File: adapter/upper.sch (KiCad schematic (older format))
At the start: 8 parts, among them J1 MALE, J2 FEMALE, J3 STANDOFF, J4 STANDOFF

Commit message: Finish schematic
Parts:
- removed D1: Red, symbol Device:LED_Small
- removed D2: Green, symbol Device:LED_Small
- removed J1: MALE, symbol Connector_Generic:Conn_02x02_Counter_Clockwise
- removed J2: FEMALE, symbol Connector_Generic:Conn_02x02_Counter_Clockwise
- removed J3, J4: STANDOFF, symbol Connector_Generic:Conn_01x01
- removed R1, R2: 1k, symbol Device:R_Small_US
- added J11: MALE, Connector_PinHeader_2.54mm:PinHeader_2x02_P2.54mm_Horizontal, symbol Connector_Generic:Conn_02x02_Top_Bottom
- added J12: FEMALE, Connector_PinSocket_2.54mm:PinSocket_2x02_P2.54mm_Vertical, symbol Connector_Generic:Conn_02x02_Odd_Even
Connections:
- wire segments 21 -> 13
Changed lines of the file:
@@
 Comment4 ""
 $EndDescr
-$Comp
-L Connector_Generic:Conn_02x02_Counter_Clockwise J?
-U 1 1 5FA96B2A
-P 3650 1700
-AR Path="/5FA96B2A" Ref="J?"  Part="1"
-AR Path="/5FA6C89B/5FA96B2A" Ref="J?"  Part="1"
-AR Path="/5FA6C6C8/5FA96B2A" Ref="J1"  Part="1"
-F 0 "J1" H 3700 1917 50  0000 C CNN
-F 1 "MALE" H 3700 1826 50  0000 C CNN
-F 2 "" H 3650 1700 50  0001 C CNN
-F 3 "~" H 3650 1700 50  0001 C CNN
-	1    3650 1700
-	1    0    0    -1
-$EndComp
-$Comp
-L Connector_Generic:Conn_02x02_Counter_Clockwise J?
-U 1 1 5FA96B38
-P 3650 2200
-AR Path="/5FA96B38" Ref="J?"  Part="1"
-AR Path="/5FA6C89B/5FA96B38" Ref="J?"  Part="1"
-AR Path="/5FA6C6C8/5FA96B38" Ref="J2"  Part="1"
-F 0 "J2" H 3700 2417 50  0000 C CNN
-F 1 "FEMALE" H 3700 2326 50  0000 C CNN
-F 2 "" H 3650 2200 50  0001 C CNN
-F 3 "~" H 3650 2200 50  0001 C CNN
-	1    3650 2200
-	1    0    0    -1
-$EndComp
 Wire Wire Line
-	3450 2300 3400 2300
+	5350 2900 5150 2900
 Wire Wire Line
-	3450 2200 3350 2200
+	5150 2900 5150 3500
 Wire Wire Line
-	3450 1800 3400 1800
+	6050 3500 6050 3550
 Wire Wire Line
-	3400 1800 3400 2300
-Wire Wire Line
-	3450 1700 3350 1700
-Wire Wire Line
-	3350 1700 3350 2200
-Wire Wire Line
-	3950 2300 4000 2300
-Wire Wire Line
-	4050 2300 4050 2350
-Wire Wire Line
-	3950 2200 4050 2200
-Wire Wire Line
-	3950 1800 4000 1800
-Wire Wire Line
-	4000 1800 4000 2300
-Connection ~ 4000 2300
-Wire Wire Line
-	4000 2300 4050 2300
-Wire Wire Line
-	3950 1700 4050 1700
-Wire Wire Line
-	4050 1700 4050 2200
+	5850 3000 5950 3000
 $Comp
 L power:+5V #PWR?
-U 1 1 5FA96B54
-P 3350 1650
-AR Path="/5FA6C89B/5FA96B54" Ref="#PWR?"  Part="1"
-AR Path="/5FA6C6C8/5FA96B54" Ref="#PWR?"  Part="1"
-F 0 "#PWR?" H 3350 1500 50  0001 C CNN
-F 1 "+5V" H 3365 1823 50  0000 C CNN
-F 2 "" H 3350 1650 50  0001 C CNN
-F 3 "" H 3350 1650 50  0001 C CNN
-	1    3350 1650
+U 1 1 5FB6CCB3
+P 5150 2900
+AR Path="/5FA6C89B/5FB6CCB3" Ref="#PWR?"  Part="1"
+AR Path="/5FA6C6C8/5FB6CCB3" Ref="#PWR0110"  Part="1"
+F 0 "#PWR0110" H 5150 2750 50  0001 C CNN
+F 1 "+5V" H 5165 3073 50  0000 C CNN
+F 2 "" H 5150 2900 50  0001 C CNN
+F 3 "" H 5150 2900 50  0001 C CNN
+	1    5150 2900
 	1    0    0    -1
 $EndComp
 $Comp
 L power:GND #PWR?
-U 1 1 5FA96B5A
-P 4050 2350
-AR Path="/5FA6C89B/5FA96B5A" Ref="#PWR?"  Part="1"
-AR Path="/5FA6C6C8/5FA96B5A" Ref="#PWR?"  Part="1"
-F 0 "#PWR?" H 4050 2100 50  0001 C CNN
-F 1 "GND" H 4050 2200 50  0000 C CNN
-F 2 "" H 4050 2350 50  0001 C CNN
-F 3 "" H 4050 2350 50  0001 C CNN
-	1    4050 2350
+U 1 1 5FB6CCB9
+P 6050 3550
+AR Path="/5FA6C89B/5FB6CCB9" Ref="#PWR?"  Part="1"
+AR Path="/5FA6C6C8/5FB6CCB9" Ref="#PWR0111"  Part="1"
+F 0 "#PWR0111" H 6050 3300 50  0001 C CNN
+F 1 "GND" H 6050 3400 50  0000 C CNN
+F 2 "" H 6050 3550 50  0001 C CNN
+F 3 "" H 6050 3550 50  0001 C CNN
+	1    6050 3550
 	1    0    0    -1
 $EndComp
 $Comp
-L Connector_Generic:Conn_01x01 J?
-U 1 1 5FA96B62
-P 3200 4300
-AR Path="/5FA6C89B/5FA96B62" Ref="J?"  Part="1"
-AR Path="/5FA6C6C8/5FA96B62" Ref="J3"  Part="1"
-F 0 "J3" V 3350 4250 50  0000 L CNN
-F 1 "STANDOFF" V 3450 4150 50  0000 L CNN
-F 2 "" H 3200 4300 50  0001 C CNN
-F 3 "~" H 3200 4300 50  0001 C CNN
-	1    3200 4300
-	0    1    1    0
-$EndComp
-$Comp
-L Connector_Generic:Conn_01x01 J?
-U 1 1 5FA96B68
-P 4150 4300
-AR Path="/5FA6C89B/5FA96B68" Ref="J?"  Part="1"
-AR Path="/5FA6C6C8/5FA96B68" Ref="J4"  Part="1"
-F 0 "J4" V 4300 4250 50  0000 L CNN
-F 1 "STANDOFF" V 4400 4150 50  0000 L CNN
-F 2 "" H 4150 4300 50  0001 C CNN
-F 3 "~" H 4150 4300 50  0001 C CNN
-	1    4150 4300
-	0    1    1    0
-$EndComp
-$Comp
-L power:+5V #PWR?
-U 1 1 5FA97846
-P 3200 3150
-AR Path="/5FA6C89B/5FA97846" Ref="#PWR?"  Part="1"
-AR Path="/5FA6C6C8/5FA97846" Ref="#PWR?"  Part="1"
-F 0 "#PWR?" H 3200 3000 50  0001 C CNN
-F 1 "+5V" H 3215 3323 50  0000 C CNN
-F 2 "" H 3200 3150 50  0001 C CNN
-F 3 "" H 3200 3150 50  0001 C CNN
-	1    3200 3150
+L Connector_Generic:Conn_02x02_Top_Bottom J?
+U 1 1 5FB6CCC1
+P 5550 2900
+AR Path="/5FB6CCC1" Ref="J?"  Part="1"
+AR Path="/5FA6C89B/5FB6CCC1" Ref="J?"  Part="1"
+AR Path="/5FA6C6C8/5FB6CCC1" Ref="J11"  Part="1"
+F 0 "J11" H 5600 3117 50  0000 C CNN
+F 1 "MALE" H 5600 3026 50  0000 C CNN
+F 2 "Connector_PinHeader_2.54mm:PinHeader_2x02_P2.54mm_Horizontal" H 5550 2900 50  0001 C CNN
+F 3 "~" H 5550 2900 50  0001 C CNN
+	1    5550 2900
 	1    0    0    -1
 $EndComp
 $Comp
-L Device:R_Small_US R1
-U 1 1 5FA97B4B
-P 3200 3450
-F 0 "R1" H 3268 3496 50  0000 L CNN
-F 1 "1k" H 3268 3405 50  0000 L CNN
-F 2 "" H 3200 3450 50  0001 C CNN
-F 3 "~" H 3200 3450 50  0001 C CNN
-	1    3200 3450
-	1    0    0    -1
-$EndComp
-$Comp
-L Device:LED_Small D1
-U 1 1 5FA97E69
-P 3200 3800
-F 0 "D1" V 3246 3730 50  0000 R CNN
-F 1 "Red" V 3155 3730 50  0000 R CNN
-F 2 "" V 3200 3800 50  0001 C CNN
-F 3 "~" V 3200 3800 50  0001 C CNN
-	1    3200 3800
-	0    -1   -1   0
-$EndComp
-Wire Wire Line
-	3200 3150 3200 3350
-Wire Wire Line
-	3200 3550 3200 3700
-Wire Wire Line
-	3200 3900 3200 4100
-$Comp
-L Device:LED_Small D2
-U 1 1 5FA99B4F
-P 4150 3800
-F 0 "D2" V 4196 3730 50  0000 R CNN
-F 1 "Green" V 4105 3730 50  0000 R CNN
-F 2 "" V 4150 3800 50  0001 C CNN
-F 3 "~" V 4150 3800 50  0001 C CNN
-	1    4150 3800
-	0    -1   -1   0
-$EndComp
-$Comp
-L Device:R_Small_US R2
-U 1 1 5FA99CCA
-P 4150 3450
-F 0 "R2" H 4218 3496 50  0000 L CNN
-F 1 "1k" H 4218 3405 50  0000 L CNN
-F 2 "" H 4150 3450 50  0001 C CNN
-F 3 "~" H 4150 3450 50  0001 C CNN
-	1    4150 3450
-	1    0    0    -1
-$EndComp
-$Comp
-L power:+5V #PWR?
-U 1 1 5FA99E18
-P 4150 3150
-AR Path="/5FA6C89B/5FA99E18" Ref="#PWR?"  Part="1"
-AR Path="/5FA6C6C8/5FA99E18" Ref="#PWR?"  Part="1"
-F 0 "#PWR?" H 4150 3000 50  0001 C CNN
-F 1 "+5V" H 4165 3323 50  0000 C CNN
-F 2 "" H 4150 3150 50  0001 C CNN
-F 3 "" H 4150 3150 50  0001 C CNN
-	1    4150 3150
+L Connector_Generic:Conn_02x02_Odd_Even J?
+U 1 1 5FB6CCC7
+P 5550 3400
+AR Path="/5FB6CCC7" Ref="J?"  Part="1"
+AR Path="/5FA6C89B/5FB6CCC7" Ref="J?"  Part="1"
+AR Path="/5FA6C6C8/5FB6CCC7" Ref="J12"  Part="1"
+F 0 "J12" H 5600 3617 50  0000 C CNN
+F 1 "FEMALE" H 5600 3526 50  0000 C CNN
+F 2 "Connector_PinSocket_2.54mm:PinSocket_2x02_P2.54mm_Vertical" H 5550 3400 50  0001 C CNN
+F 3 "~" H 5550 3400 50  0001 C CNN
+	1    5550 3400
 	1    0    0    -1
 $EndComp
 Wire Wire Line
-	4150 3350 4150 3150
+	5850 3500 6050 3500
 Wire Wire Line
-	4150 3550 4150 3700
+	5850 3400 5950 3400
 Wire Wire Line
-	4150 3900 4150 4100
+	5950 3000 5950 3400
 Wire Wire Line
-	3350 1650 3350 1700
-Connection ~ 3350 1700
+	5850 2900 6050 2900
+Wire Wire Line
+	6050 2900 6050 3500
+Connection ~ 6050 3500
+Connection ~ 5150 2900
+Wire Wire Line
+	5350 3000 5250 3000
+Wire Wire Line
+	5150 3500 5350 3500
+Wire Wire Line
+	5250 3000 5250 3400
+Wire Wire Line
+	5250 3400 5350 3400
 $EndSCHEMATC

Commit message: Change female headers to horizontal
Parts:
- J12: footprint Connector_PinSocket_2.54mm:PinSocket_2x02_P2.54mm_Vertical -> Connector_PinSocket_2.54mm:PinSocket_2x02_P2.54mm_Horizontal
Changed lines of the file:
@@
 F 0 "J12" H 5600 3617 50  0000 C CNN
 F 1 "FEMALE" H 5600 3526 50  0000 C CNN
-F 2 "Connector_PinSocket_2.54mm:PinSocket_2x02_P2.54mm_Vertical" H 5550 3400 50  0001 C CNN
+F 2 "Connector_PinSocket_2.54mm:PinSocket_2x02_P2.54mm_Horizontal" H 5550 3400 50  0001 C CNN
 F 3 "~" H 5550 3400 50  0001 C CNN
 	1    5550 3400

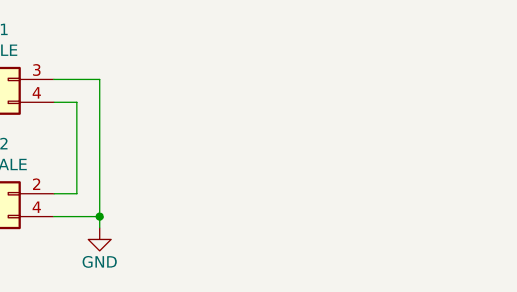
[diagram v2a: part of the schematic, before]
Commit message: Add holes for standoffs
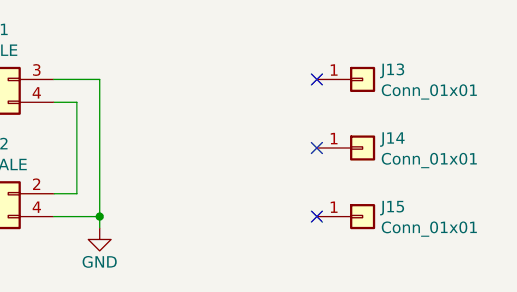
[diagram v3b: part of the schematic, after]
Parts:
- added J13, J14, J15: Conn_01x01, MountingHole:MountingHole_2.2mm_M2_Pad_Via, symbol Connector_Generic:Conn_01x01
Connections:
- no-connect marks 0 -> 3
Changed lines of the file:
@@
 Wire Wire Line
 	5250 3400 5350 3400
+$Comp
+L Connector_Generic:Conn_01x01 J?
+U 1 1 5FB93146
+P 7200 2900
+AR Path="/5FA6C89B/5FB93146" Ref="J?"  Part="1"
+AR Path="/5FA6C6C8/5FB93146" Ref="J13"  Part="1"
+F 0 "J13" H 7280 2942 50  0000 L CNN
+F 1 "Conn_01x01" H 7280 2851 50  0000 L CNN
+F 2 "MountingHole:MountingHole_2.2mm_M2_Pad_Via" H 7200 2900 50  0001 C CNN
+F 3 "~" H 7200 2900 50  0001 C CNN
+	1    7200 2900
+	1    0    0    -1
+$EndComp
+NoConn ~ 7000 2900
+$Comp
+L Connector_Generic:Conn_01x01 J?
+U 1 1 5FB9314D
+P 7200 3200
+AR Path="/5FA6C89B/5FB9314D" Ref="J?"  Part="1"
+AR Path="/5FA6C6C8/5FB9314D" Ref="J14"  Part="1"
+F 0 "J14" H 7280 3242 50  0000 L CNN
+F 1 "Conn_01x01" H 7280 3151 50  0000 L CNN
+F 2 "MountingHole:MountingHole_2.2mm_M2_Pad_Via" H 7200 3200 50  0001 C CNN
+F 3 "~" H 7200 3200 50  0001 C CNN
+	1    7200 3200
+	1    0    0    -1
+$EndComp
+$Comp
+L Connector_Generic:Conn_01x01 J?
+U 1 1 5FB93153
+P 7200 3500
+AR Path="/5FA6C89B/5FB93153" Ref="J?"  Part="1"
+AR Path="/5FA6C6C8/5FB93153" Ref="J15"  Part="1"
+F 0 "J15" H 7280 3542 50  0000 L CNN
+F 1 "Conn_01x01" H 7280 3451 50  0000 L CNN
+F 2 "MountingHole:MountingHole_2.2mm_M2_Pad_Via" H 7200 3500 50  0001 C CNN
+F 3 "~" H 7200 3500 50  0001 C CNN
+	1    7200 3500
+	1    0    0    -1
+$EndComp
+NoConn ~ 7000 3200
+NoConn ~ 7000 3500
 $EndSCHEMATC

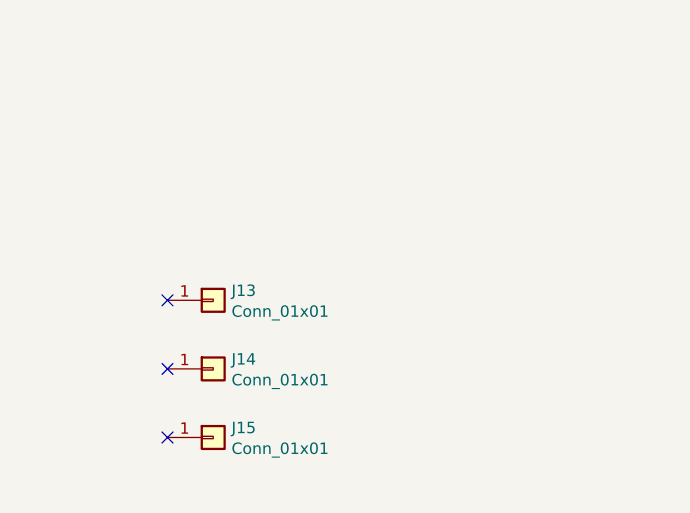
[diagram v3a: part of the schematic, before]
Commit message: Move LEDs to upper board
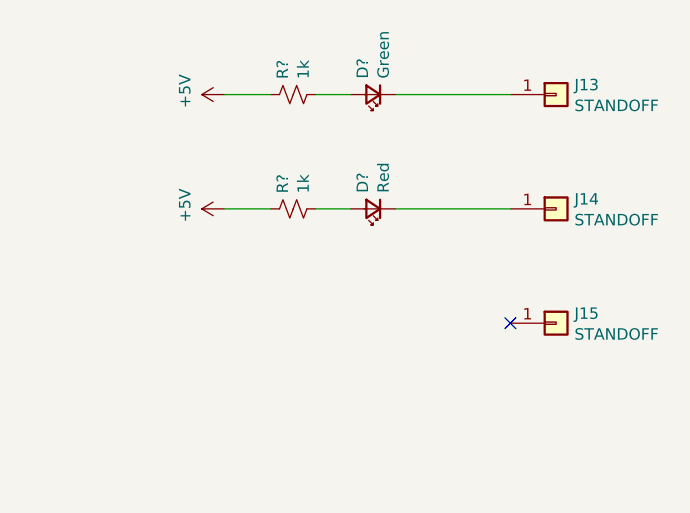
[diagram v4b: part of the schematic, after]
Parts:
- added D?: Red, LED_SMD:LED_0805_2012Metric_Pad1.15x1.40mm_HandSolder, symbol Device:LED_Small
- added D?: Green, LED_SMD:LED_0805_2012Metric_Pad1.15x1.40mm_HandSolder, symbol Device:LED_Small
- added R? (x2): 1k, Resistor_SMD:R_0805_2012Metric_Pad1.20x1.40mm_HandSolder, symbol Device:R_Small_US
- J13, J14, J15: value Conn_01x01 -> STANDOFF
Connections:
- net +5V: now also R?.1, R?.1
- net at J13.1 (Pin_1): now also D?.1 (K)
- net at J14.1 (Pin_1): now also D?.1 (K)
- new net: D?.2 (A), R?.2 (x2)
- no-connect marks 3 -> 1
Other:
- moved on the sheet: J13, J14, J15
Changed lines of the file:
@@
 L Connector_Generic:Conn_01x01 J?
 U 1 1 5FB93146
-P 7200 2900
+P 8700 2000
 AR Path="/5FA6C89B/5FB93146" Ref="J?"  Part="1"
 AR Path="/5FA6C6C8/5FB93146" Ref="J13"  Part="1"
-F 0 "J13" H 7280 2942 50  0000 L CNN
-F 1 "Conn_01x01" H 7280 2851 50  0000 L CNN
-F 2 "MountingHole:MountingHole_2.2mm_M2_Pad_Via" H 7200 2900 50  0001 C CNN
-F 3 "~" H 7200 2900 50  0001 C CNN
-	1    7200 2900
+F 0 "J13" H 8780 2042 50  0000 L CNN
+F 1 "STANDOFF" H 8780 1951 50  0000 L CNN
+F 2 "MountingHole:MountingHole_2.2mm_M2_Pad_Via" H 8700 2000 50  0001 C CNN
+F 3 "~" H 8700 2000 50  0001 C CNN
+	1    8700 2000
 	1    0    0    -1
 $EndComp
-NoConn ~ 7000 2900
 $Comp
 L Connector_Generic:Conn_01x01 J?
 U 1 1 5FB9314D
-P 7200 3200
+P 8700 2500
 AR Path="/5FA6C89B/5FB9314D" Ref="J?"  Part="1"
 AR Path="/5FA6C6C8/5FB9314D" Ref="J14"  Part="1"
-F 0 "J14" H 7280 3242 50  0000 L CNN
-F 1 "Conn_01x01" H 7280 3151 50  0000 L CNN
-F 2 "MountingHole:MountingHole_2.2mm_M2_Pad_Via" H 7200 3200 50  0001 C CNN
-F 3 "~" H 7200 3200 50  0001 C CNN
-	1    7200 3200
+F 0 "J14" H 8780 2542 50  0000 L CNN
+F 1 "STANDOFF" H 8780 2451 50  0000 L CNN
+F 2 "MountingHole:MountingHole_2.2mm_M2_Pad_Via" H 8700 2500 50  0001 C CNN
+F 3 "~" H 8700 2500 50  0001 C CNN
+	1    8700 2500
 	1    0    0    -1
 $EndComp
@@
 L Connector_Generic:Conn_01x01 J?
 U 1 1 5FB93153
-P 7200 3500
+P 8700 3000
 AR Path="/5FA6C89B/5FB93153" Ref="J?"  Part="1"
 AR Path="/5FA6C6C8/5FB93153" Ref="J15"  Part="1"
-F 0 "J15" H 7280 3542 50  0000 L CNN
-F 1 "Conn_01x01" H 7280 3451 50  0000 L CNN
-F 2 "MountingHole:MountingHole_2.2mm_M2_Pad_Via" H 7200 3500 50  0001 C CNN
-F 3 "~" H 7200 3500 50  0001 C CNN
-	1    7200 3500
+F 0 "J15" H 8780 3042 50  0000 L CNN
+F 1 "STANDOFF" H 8780 2951 50  0000 L CNN
+F 2 "MountingHole:MountingHole_2.2mm_M2_Pad_Via" H 8700 3000 50  0001 C CNN
+F 3 "~" H 8700 3000 50  0001 C CNN
+	1    8700 3000
 	1    0    0    -1
 $EndComp
-NoConn ~ 7000 3200
-NoConn ~ 7000 3500
+NoConn ~ 8500 3000
+$Comp
+L power:+5V #PWR?
+U 1 1 5FBB343F
+P 7250 2500
+AR Path="/5FA6C89B/5FBB343F" Ref="#PWR?"  Part="1"
+AR Path="/5FA6C6C8/5FBB343F" Ref="#PWR?"  Part="1"
+F 0 "#PWR?" H 7250 2350 50  0001 C CNN
+F 1 "+5V" H 7265 2673 50  0000 C CNN
+F 2 "" H 7250 2500 50  0001 C CNN
+F 3 "" H 7250 2500 50  0001 C CNN
+	1    7250 2500
+	0    -1   -1   0
+$EndComp
+$Comp
+L Device:R_Small_US R?
+U 1 1 5FBB3445
+P 7550 2500
+AR Path="/5FA6C6C8/5FBB3445" Ref="R?"  Part="1"
+AR Path="/5FA6C89B/5FBB3445" Ref="R?"  Part="1"
+F 0 "R?" H 7618 2546 50  0000 L CNN
+F 1 "1k" H 7618 2455 50  0000 L CNN
+F 2 "Resistor_SMD:R_0805_2012Metric_Pad1.20x1.40mm_HandSolder" H 7550 2500 50  0001 C CNN
+F 3 "~" H 7550 2500 50  0001 C CNN
+	1    7550 2500
+	0    -1   -1   0
+$EndComp
+$Comp
+L Device:LED_Small D?
+U 1 1 5FBB344B
+P 7900 2500
+AR Path="/5FA6C6C8/5FBB344B" Ref="D?"  Part="1"
+AR Path="/5FA6C89B/5FBB344B" Ref="D?"  Part="1"
+F 0 "D?" V 7946 2430 50  0000 R CNN
+F 1 "Red" V 7855 2430 50  0000 R CNN
+F 2 "LED_SMD:LED_0805_2012Metric_Pad1.15x1.40mm_HandSolder" V 7900 2500 50  0001 C CNN
+F 3 "~" V 7900 2500 50  0001 C CNN
+	1    7900 2500
+	-1   0    0    1
+$EndComp
+Wire Wire Line
+	7250 2500 7450 2500
+Wire Wire Line
+	7650 2500 7800 2500
+$Comp
+L Device:LED_Small D?
+U 1 1 5FBB3453
+P 7900 2000
+AR Path="/5FA6C6C8/5FBB3453" Ref="D?"  Part="1"
+AR Path="/5FA6C89B/5FBB3453" Ref="D?"  Part="1"
+F 0 "D?" V 7946 1930 50  0000 R CNN
+F 1 "Green" V 7855 1930 50  0000 R CNN
+F 2 "LED_SMD:LED_0805_2012Metric_Pad1.15x1.40mm_HandSolder" V 7900 2000 50  0001 C CNN
+F 3 "~" V 7900 2000 50  0001 C CNN
+	1    7900 2000
+	-1   0    0    1
+$EndComp
+$Comp
+L Device:R_Small_US R?
+U 1 1 5FBB3459
+P 7550 2000
+AR Path="/5FA6C6C8/5FBB3459" Ref="R?"  Part="1"
+AR Path="/5FA6C89B/5FBB3459" Ref="R?"  Part="1"
+F 0 "R?" H 7618 2046 50  0000 L CNN
+F 1 "1k" H 7618 1955 50  0000 L CNN
+F 2 "Resistor_SMD:R_0805_2012Metric_Pad1.20x1.40mm_HandSolder" H 7550 2000 50  0001 C CNN
+F 3 "~" H 7550 2000 50  0001 C CNN
+	1    7550 2000
+	0    -1   -1   0
+$EndComp
+$Comp
+L power:+5V #PWR?
+U 1 1 5FBB345F
+P 7250 2000
+AR Path="/5FA6C89B/5FBB345F" Ref="#PWR?"  Part="1"
+AR Path="/5FA6C6C8/5FBB345F" Ref="#PWR?"  Part="1"
+F 0 "#PWR?" H 7250 1850 50  0001 C CNN
+F 1 "+5V" H 7265 2173 50  0000 C CNN
+F 2 "" H 7250 2000 50  0001 C CNN
+F 3 "" H 7250 2000 50  0001 C CNN
+	1    7250 2000
+	0    -1   -1   0
+$EndComp
+Wire Wire Line
+	7450 2000 7250 2000
+Wire Wire Line
+	7650 2000 7800 2000
+Wire Wire Line
+	8000 2000 8500 2000
+Wire Wire Line
+	8000 2500 8500 2500
 $EndSCHEMATC

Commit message: Annotate
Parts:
- gave numbers to parts that had none: 4
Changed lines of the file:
@@
 P 7250 2500
 AR Path="/5FA6C89B/5FBB343F" Ref="#PWR?"  Part="1"
-AR Path="/5FA6C6C8/5FBB343F" Ref="#PWR?"  Part="1"
-F 0 "#PWR?" H 7250 2350 50  0001 C CNN
+AR Path="/5FA6C6C8/5FBB343F" Ref="#PWR0108"  Part="1"
+F 0 "#PWR0108" H 7250 2350 50  0001 C CNN
 F 1 "+5V" H 7265 2673 50  0000 C CNN
 F 2 "" H 7250 2500 50  0001 C CNN
@@
 $EndComp
 $Comp
-L Device:R_Small_US R?
+L Device:R_Small_US R2
 U 1 1 5FBB3445
 P 7550 2500
-AR Path="/5FA6C6C8/5FBB3445" Ref="R?"  Part="1"
+AR Path="/5FA6C6C8/5FBB3445" Ref="R2"  Part="1"
 AR Path="/5FA6C89B/5FBB3445" Ref="R?"  Part="1"
-F 0 "R?" H 7618 2546 50  0000 L CNN
+F 0 "R2" H 7618 2546 50  0000 L CNN
 F 1 "1k" H 7618 2455 50  0000 L CNN
 F 2 "Resistor_SMD:R_0805_2012Metric_Pad1.20x1.40mm_HandSolder" H 7550 2500 50  0001 C CNN
@@
 $EndComp
 $Comp
-L Device:LED_Small D?
+L Device:LED_Small D2
 U 1 1 5FBB344B
 P 7900 2500
-AR Path="/5FA6C6C8/5FBB344B" Ref="D?"  Part="1"
+AR Path="/5FA6C6C8/5FBB344B" Ref="D2"  Part="1"
 AR Path="/5FA6C89B/5FBB344B" Ref="D?"  Part="1"
-F 0 "D?" V 7946 2430 50  0000 R CNN
+F 0 "D2" V 7946 2430 50  0000 R CNN
 F 1 "Red" V 7855 2430 50  0000 R CNN
 F 2 "LED_SMD:LED_0805_2012Metric_Pad1.15x1.40mm_HandSolder" V 7900 2500 50  0001 C CNN
@@
 	7650 2500 7800 2500
 $Comp
-L Device:LED_Small D?
+L Device:LED_Small D1
 U 1 1 5FBB3453
 P 7900 2000
-AR Path="/5FA6C6C8/5FBB3453" Ref="D?"  Part="1"
+AR Path="/5FA6C6C8/5FBB3453" Ref="D1"  Part="1"
 AR Path="/5FA6C89B/5FBB3453" Ref="D?"  Part="1"
-F 0 "D?" V 7946 1930 50  0000 R CNN
+F 0 "D1" V 7946 1930 50  0000 R CNN
 F 1 "Green" V 7855 1930 50  0000 R CNN
 F 2 "LED_SMD:LED_0805_2012Metric_Pad1.15x1.40mm_HandSolder" V 7900 2000 50  0001 C CNN
@@
 $EndComp
 $Comp
-L Device:R_Small_US R?
+L Device:R_Small_US R1
 U 1 1 5FBB3459
 P 7550 2000
-AR Path="/5FA6C6C8/5FBB3459" Ref="R?"  Part="1"
+AR Path="/5FA6C6C8/5FBB3459" Ref="R1"  Part="1"
 AR Path="/5FA6C89B/5FBB3459" Ref="R?"  Part="1"
-F 0 "R?" H 7618 2046 50  0000 L CNN
+F 0 "R1" H 7618 2046 50  0000 L CNN
 F 1 "1k" H 7618 1955 50  0000 L CNN
 F 2 "Resistor_SMD:R_0805_2012Metric_Pad1.20x1.40mm_HandSolder" H 7550 2000 50  0001 C CNN
@@
 P 7250 2000
 AR Path="/5FA6C89B/5FBB345F" Ref="#PWR?"  Part="1"
-AR Path="/5FA6C6C8/5FBB345F" Ref="#PWR?"  Part="1"
-F 0 "#PWR?" H 7250 1850 50  0001 C CNN
+AR Path="/5FA6C6C8/5FBB345F" Ref="#PWR0109"  Part="1"
+F 0 "#PWR0109" H 7250 1850 50  0001 C CNN
 F 1 "+5V" H 7265 2173 50  0000 C CNN
 F 2 "" H 7250 2000 50  0001 C CNN

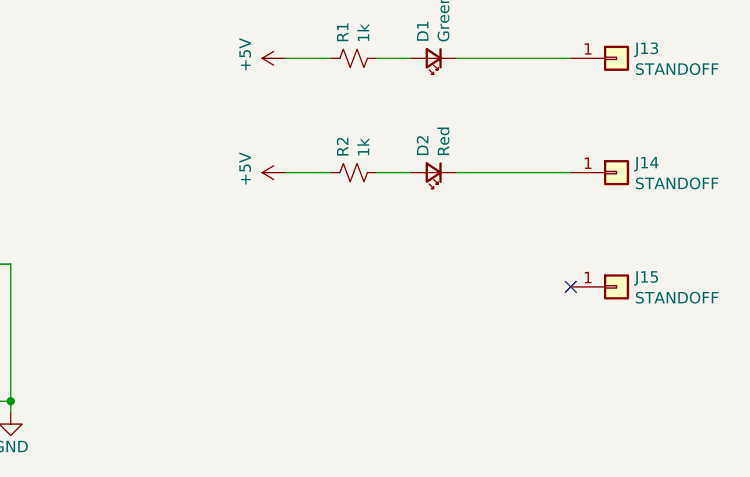
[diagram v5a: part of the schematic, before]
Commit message: Put +5V on standoff: Make LEDs work w/o connection
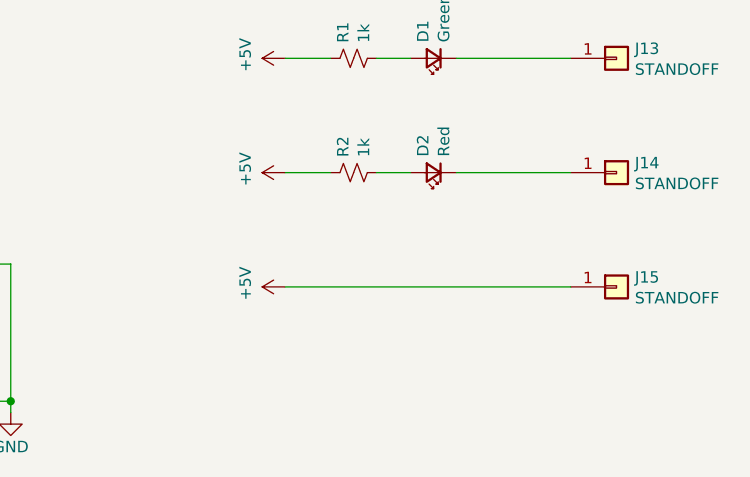
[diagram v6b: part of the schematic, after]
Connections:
- net +5V: now also J15.1 (Pin_1)
- no-connect marks 1 -> 0
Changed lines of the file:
@@
 	1    0    0    -1
 $EndComp
-NoConn ~ 8500 3000
 $Comp
 L power:+5V #PWR?
@@
 Wire Wire Line
 	8000 2500 8500 2500
+$Comp
+L power:+5V #PWR?
+U 1 1 5FC055F4
+P 7250 3000
+AR Path="/5FA6C89B/5FC055F4" Ref="#PWR?"  Part="1"
+AR Path="/5FA6C6C8/5FC055F4" Ref="#PWR?"  Part="1"
+F 0 "#PWR?" H 7250 2850 50  0001 C CNN
+F 1 "+5V" H 7265 3173 50  0000 C CNN
+F 2 "" H 7250 3000 50  0001 C CNN
+F 3 "" H 7250 3000 50  0001 C CNN
+	1    7250 3000
+	0    -1   -1   0
+$EndComp
+Wire Wire Line
+	7250 3000 8500 3000
 $EndSCHEMATC
